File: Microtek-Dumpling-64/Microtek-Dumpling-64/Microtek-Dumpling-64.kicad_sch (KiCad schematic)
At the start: 30 parts, among them J1 E5-E3, P1 AppleIIBus, P3 E6-E7, SW1 SW_DIP_x08, U11 PAL16R6, U12 27C32, U13 74LS32, U17 74LS74, U18 74LS10, U4 8741, U8 74LS04, Y1 6 MHz

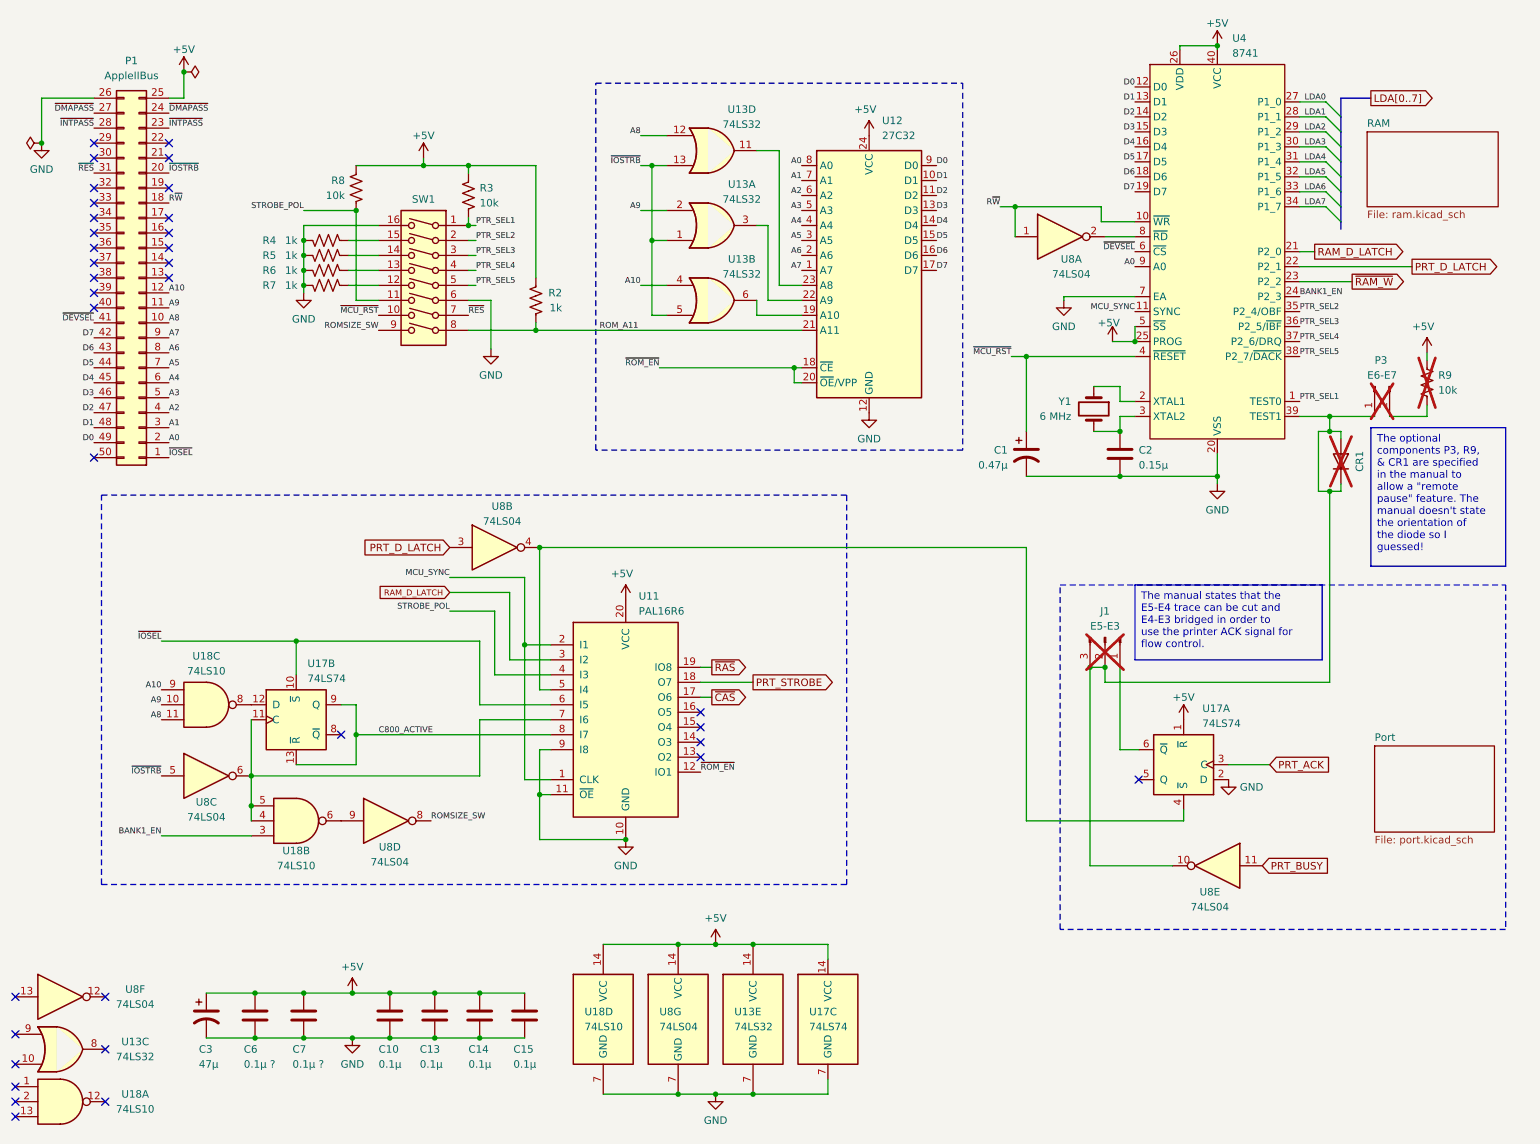
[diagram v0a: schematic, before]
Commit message: Update the Dumpling-64 project to kicad8 and the shared symbol library
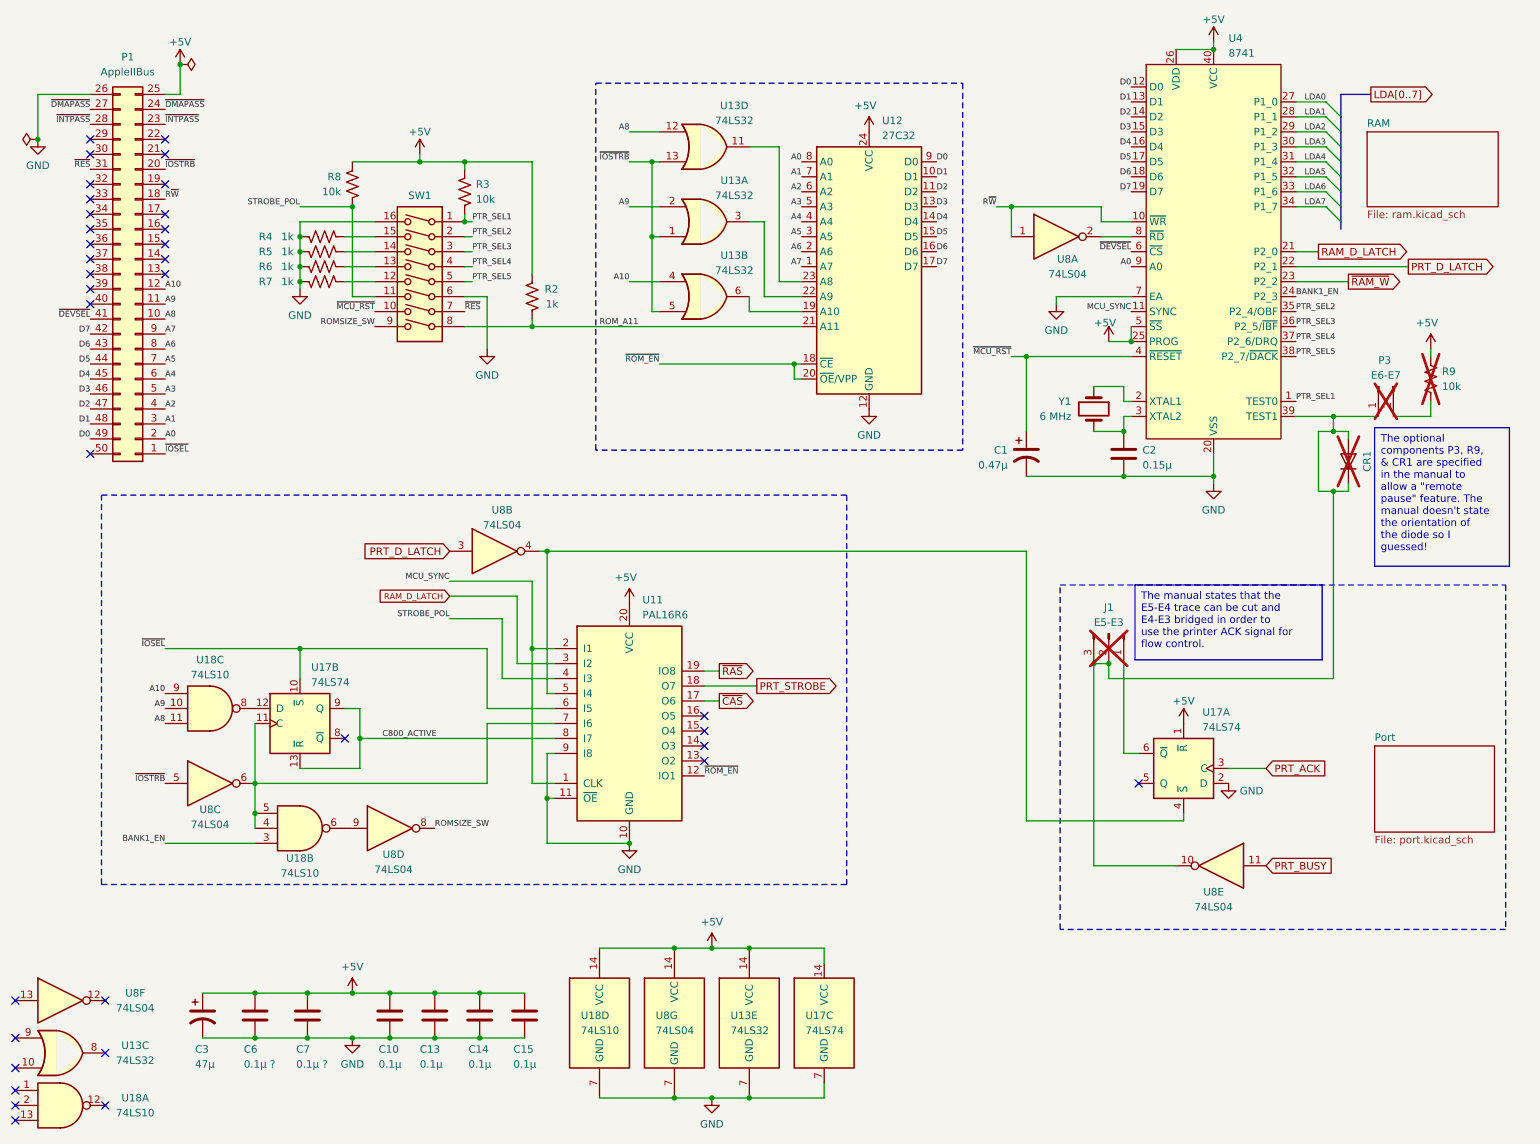
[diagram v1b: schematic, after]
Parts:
- U12: symbol Memory:27C32 -> Memory_Legacy:27C32
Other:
- moved on the sheet: C2, C3, C7, CR1, J1, P1, P3, R2, R3, R4, R5, R6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
